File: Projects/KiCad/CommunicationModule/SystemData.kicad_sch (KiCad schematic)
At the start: 33 parts, among them J1 Conn_01x08, SW1 SW_Push, U1 MCP2562-E-P, U2 MCP2515-I/P, U3 NJM7805SDL1, U4 ABX00012, Y1 8MHz

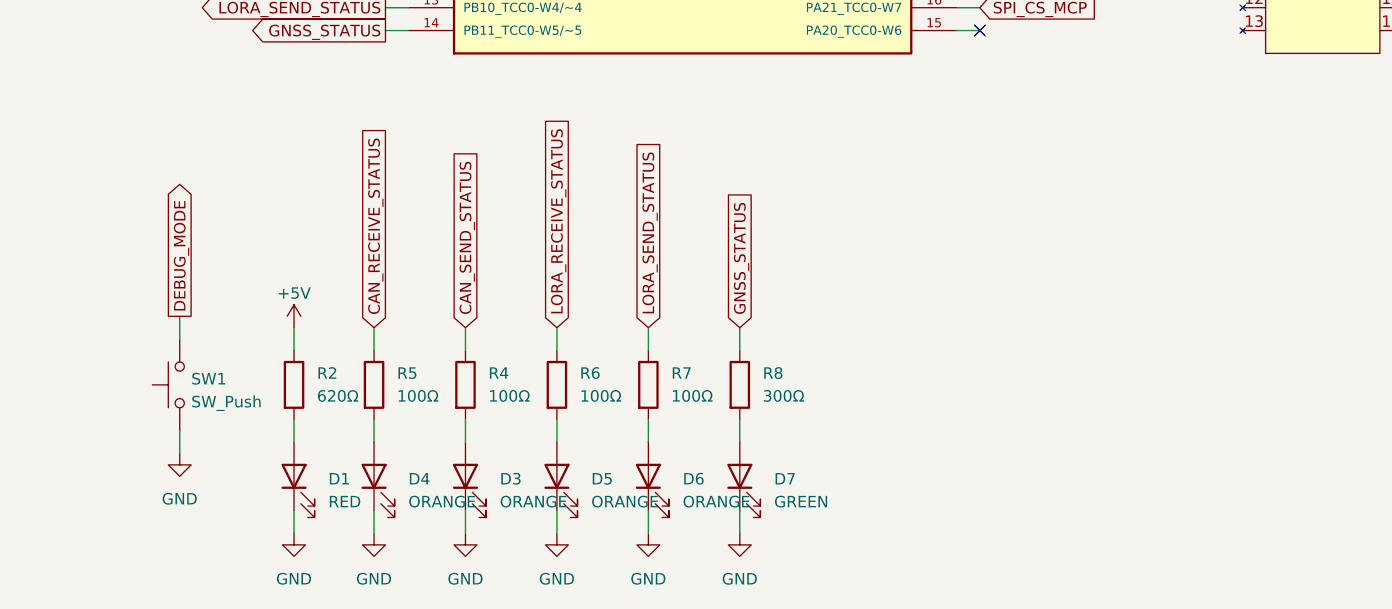
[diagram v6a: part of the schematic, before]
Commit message: スイッチをピアノスイッチに変更
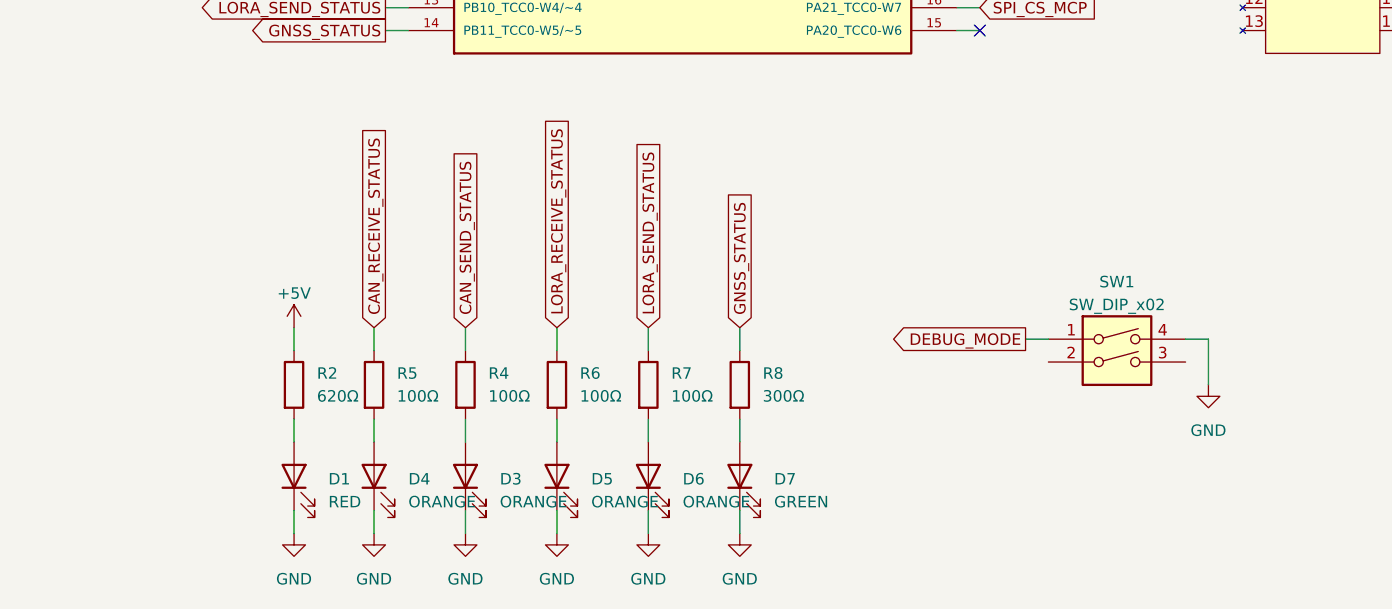
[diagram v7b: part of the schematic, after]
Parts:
- removed SW1: SW_Push, Button_Switch_THT:SW_PUSH_6mm, symbol Switch:SW_Push
- added SW1: SW_DIP_x02, Button_Switch_THT:SW_DIP_SPSTx02_Piano_10.8x6.64mm_W7.62mm_P2.54mm, symbol Switch:SW_DIP_x02
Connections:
- net DEBUG_MODE: now also SW1.1
- net GND: now also SW1.4
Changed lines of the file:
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@@
+    (stroke (width 0) (type default))
+  )
+  (wire (pts (xy 148.59 162.56) (xy 148.59 167.64))
     (stroke (width 0) (type default))
   )
@@
     (stroke (width 0) (type default))
   )
+  (wire (pts (xy 128.27 162.56) (xy 130.81 162.56))
+    (stroke (width 0) (type default))
+  )
   (wire (pts (xy 96.52 35.56) (xy 96.52 38.1))
     (stroke (width 0) (type default))
@@
     (stroke (width 0) (type default))
   )
+  (wire (pts (xy 146.05 162.56) (xy 148.59 162.56))
+    (stroke (width 0) (type default))
+  )
   (wire (pts (xy 149.86 68.58) (xy 152.4 68.58))
     (stroke (width 0) (type default))
@@
     (stroke (width 0) (type default))
   )
-  (wire (pts (xy 34.29 160.02) (xy 34.29 162.56))
-    (stroke (width 0) (type default))
-  )
   (wire (pts (xy 86.36 171.45) (xy 86.36 173.99))
     (stroke (width 0) (type default))
@@
   )
   (wire (pts (xy 250.19 110.49) (xy 250.19 113.03))
-    (stroke (width 0) (type default))
-  )
-  (wire (pts (xy 34.29 172.72) (xy 34.29 175.26))
     (stroke (width 0) (type default))
   )
@@
     )
   )
+  (global_label "DEBUG_MODE" (shape output) (at 128.27 162.56 180) (fields_autoplaced)
+    (effects (font (size 1.27 1.27)) (justify right))
+    (property "Intersheetrefs" "${INTERSHEET_REFS}" (at 112.9062 162.56 0)
+      (effects (font (size 1.27 1.27)) (justify right) hide)
+    )
+  )
   (global_label "CAN_H" (shape bidirectional) (at 80.01 49.53 180) (fields_autoplaced)
     (effects (font (size 1.27 1.27)) (justify right))
@@
     )
   )
-  (global_label "DEBUG_MODE" (shape output) (at 34.29 160.02 90) (fields_autoplaced)
-    (effects (font (size 1.27 1.27)) (justify left))
-    (property "Intersheetrefs" "${INTERSHEET_REFS}" (at 34.29 144.6562 90)
-      (effects (font (size 1.27 1.27)) (justify left) hide)
-    )
-  )
   (global_label "DEBUG_MODE" (shape input) (at 57.15 115.57 180) (fields_autoplaced)
     (effects (font (size 1.27 1.27)) (justify right))
@@
         (path "/ea1ed597-7cd3-4340-902e-bdce8f2d7a62"
           (reference "#PWR014") (unit 1)
+        )
+      )
+    )
+  )
+  (symbol (lib_id "Switch:SW_DIP_x02") (at 138.43 165.1 0) (unit 1)
+    (in_bom yes) (on_board yes) (dnp no) (fields_autoplaced)
+    (property "Reference" "SW1" (at 138.43 156.21 0)
+      (effects (font (size 1.27 1.27)))
+    )
+    (property "Value" "SW_DIP_x02" (at 138.43 158.75 0)
+      (effects (font (size 1.27 1.27)))
+    )
+    (property "Footprint" "Button_Switch_THT:SW_DIP_SPSTx02_Piano_10.8x6.64mm_W7.62mm_P2.54mm" (at 138.43 165.1 0)
+      (effects (font (size 1.27 1.27)) hide)
+    )
+    (property "Datasheet" "~" (at 138.43 165.1 0)
+      (effects (font (size 1.27 1.27)) hide)
+    )
+    (pin "1")
+    (pin "2")
+    (pin "3")
+    (pin "4")
+    (instances
+      (project "SystemData"
+        (path "/ea1ed597-7cd3-4340-902e-bdce8f2d7a62"
+          (reference "SW1") (unit 1)
         )
       )
@@
     )
   )
-  (symbol (lib_id "power:GND") (at 34.29 175.26 0) (mirror y) (unit 1)
-    (in_bom yes) (on_board yes) (dnp no) (fields_autoplaced)
-    (property "Reference" "#PWR018" (at 34.29 181.61 0)
-      (effects (font (size 1.27 1.27)) hide)
-    )
-    (property "Value" "GND" (at 34.29 180.34 0)
-      (effects (font (size 1.27 1.27)))
-    )
-    (property "Footprint" "" (at 34.29 175.26 0)
-      (effects (font (size 1.27 1.27)) hide)
-    )
-    (property "Datasheet" "" (at 34.29 175.26 0)
-      (effects (font (size 1.27 1.27)) hide)
-    )
-    (pin "1")
-    (instances
-      (project "SystemData"
-        (path "/ea1ed597-7cd3-4340-902e-bdce8f2d7a62"
-          (reference "#PWR018") (unit 1)
-        )
-      )
-    )
-  )
   (symbol (lib_id "power:+3.3V") (at 96.52 25.4 0) (unit 1)
     (in_bom yes) (on_board yes) (dnp no) (fields_autoplaced)
@@
         (path "/ea1ed597-7cd3-4340-902e-bdce8f2d7a62"
           (reference "C6") (unit 1)
+        )
+      )
+    )
+  )
+  (symbol (lib_id "power:GND") (at 148.59 167.64 0) (mirror y) (unit 1)
+    (in_bom yes) (on_board yes) (dnp no) (fields_autoplaced)
+    (property "Reference" "#PWR018" (at 148.59 173.99 0)
+      (effects (font (size 1.27 1.27)) hide)
+    )
+    (property "Value" "GND" (at 148.59 172.72 0)
+      (effects (font (size 1.27 1.27)))
+    )
+    (property "Footprint" "" (at 148.59 167.64 0)
+      (effects (font (size 1.27 1.27)) hide)
+    )
+    (property "Datasheet" "" (at 148.59 167.64 0)
+      (effects (font (size 1.27 1.27)) hide)
+    )
+    (pin "1")
+    (instances
+      (project "SystemData"
+        (path "/ea1ed597-7cd3-4340-902e-bdce8f2d7a62"
+          (reference "#PWR018") (unit 1)
         )
       )
@@
         )
       )
-    )
-  )
-  (symbol (lib_id "Switch:SW_Push") (at 34.29 167.64 90) (unit 1)
-    (in_bom yes) (on_board yes) (dnp no) (fields_autoplaced)
-    (property "Reference" "SW1" (at 35.56 167.005 90)
-      (effects (font (size 1.27 1.27)) (justify right))
-    )
-    (property "Value" "SW_Push" (at 35.56 169.545 90)
-      (effects (font (size 1.27 1.27)) (justify right))
-    )
-    (property "Footprint" "Button_Switch_THT:SW_PUSH_6mm" (at 29.21 167.64 0)
-      (effects (font (size 1.27 1.27)) hide)
-    )
-    (property "Datasheet" "~" (at 29.21 167.64 0)
-      (effects (font (size 1.27 1.27)) hide)
-    )
-    (pin "1")
-    (pin "2")
-    (instances
-      (project "SystemData"
-        (path "/ea1ed597-7cd3-4340-902e-bdce8f2d7a62"
-          (reference "SW1") (unit 1)
-        )
-      )

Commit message: 三端子レギュレータをTO-252-3からTO-252-2に変更
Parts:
- U3: footprint Package_TO_SOT_SMD:TO-252-3_TabPin2 -> Package_TO_SOT_SMD:TO-252-2
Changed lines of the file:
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@@
       (effects (font (size 1.27 1.27)))
     )
-    (property "Footprint" "Package_TO_SOT_SMD:TO-252-3_TabPin2" (at 225.425 104.14 0)
+    (property "Footprint" "Package_TO_SOT_SMD:TO-252-2" (at 225.425 104.14 0)
       (effects (font (size 1.27 1.27) italic) (justify left) hide)
     )
